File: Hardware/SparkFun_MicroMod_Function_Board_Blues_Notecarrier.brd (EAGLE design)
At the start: 37.5 x 65 mm, 85 parts, among them J2 MICROMOD_FUNCTION_STANDARD, J6 NOTECARD, Q1 5.8A/30V/35mΩ, Q2 20V/4.2A/52mΩ/1.4W, Q3 5.8A/30V/35mΩ, Q4 20V/4.2A/52mΩ/1.4W, U1 EEPROM, U2 TCR2EF33

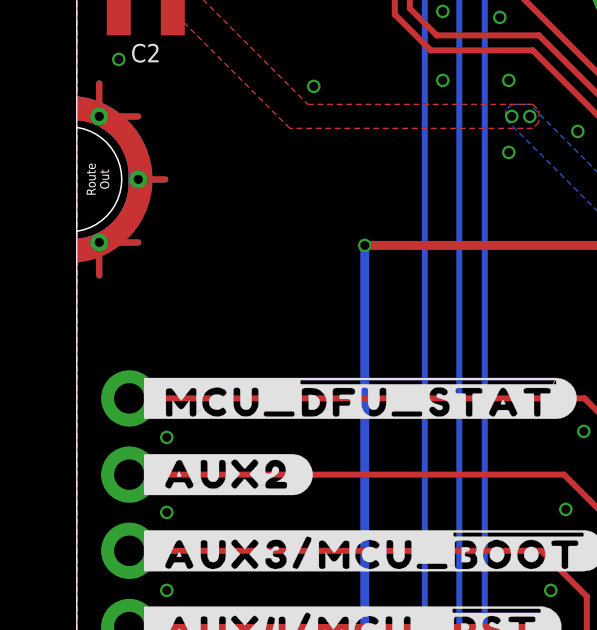
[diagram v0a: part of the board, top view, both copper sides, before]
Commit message: Added micromod silks.
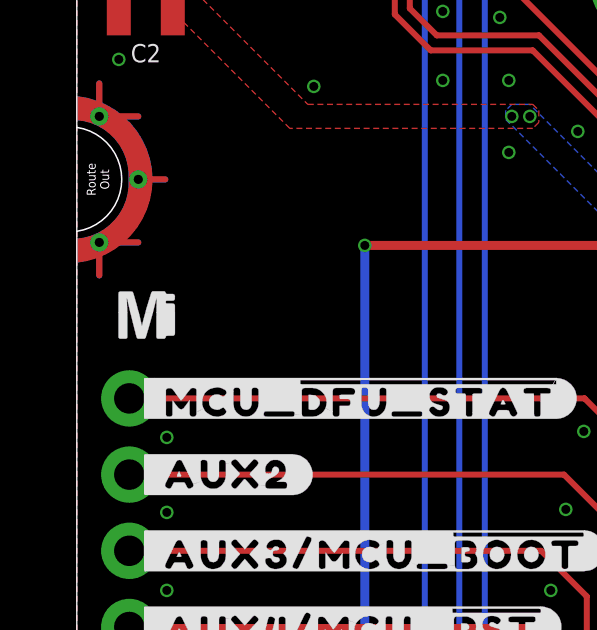
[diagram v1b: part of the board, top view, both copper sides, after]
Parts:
- added U$29: (no value), SparkFun-MicroMod:MICROMOD_MI_LOGO_.35
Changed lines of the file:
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@@
 <element name="U$27" library="output" package="#AUX1#MCU_#DFU_STAT##0" value="" x="21.2" y="36.7" smashed="yes" rot="MR0"/>
 <element name="U$28" library="SparkFun-MicroMod" package="MICROMOD_LOGO_.3" value="" x="20.2" y="41.1" smashed="yes" rot="MR0"/>
+<element name="U$29" library="SparkFun-MicroMod" package="MICROMOD_MI_LOGO_.35" value="" x="2.3" y="39.5" smashed="yes"/>
 </elements>
 <signals>

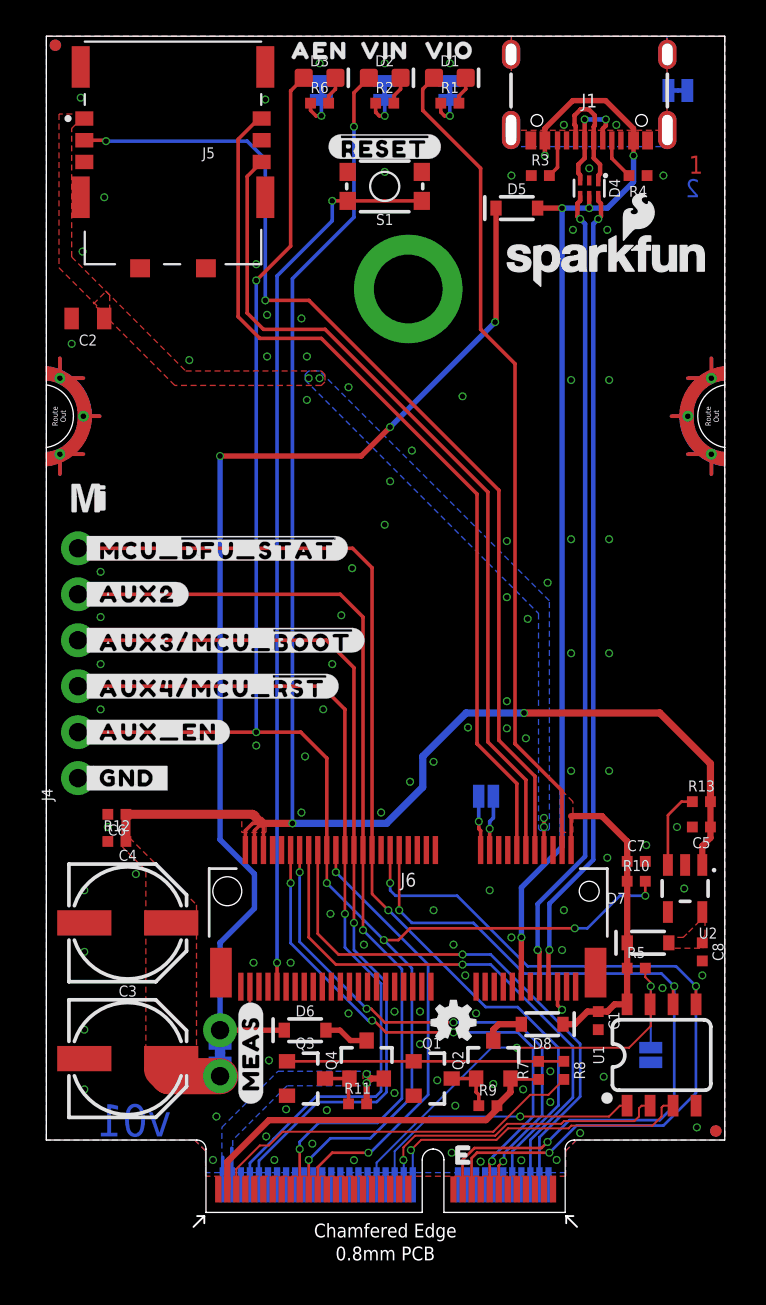
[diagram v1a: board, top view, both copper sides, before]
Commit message: Post DR updates.
Schematic:
Add Text to VREG
Add Text to Notecard
add 100 ohm resistor on pwr ctrl
Change Q1/Q3 transistors
Add Text to jumpers
Move V_USB on Notecard

Board:
Remove L2/L15
Add units for measures
Remove underscores from Silks
Move EWP via over
Remove copper layer notes
Give silk labels correct pointers
Increase mask stop on pads to ensure isolation
Move V_USB via down to allow ground pour
Check Wire stubs
Move 3.3V up to pour gnd better
Redo measures to make them look nice
Move some vias around to pour ground better
Place 100 ohm resistors
Place InRush current limiting resistor
Reroute
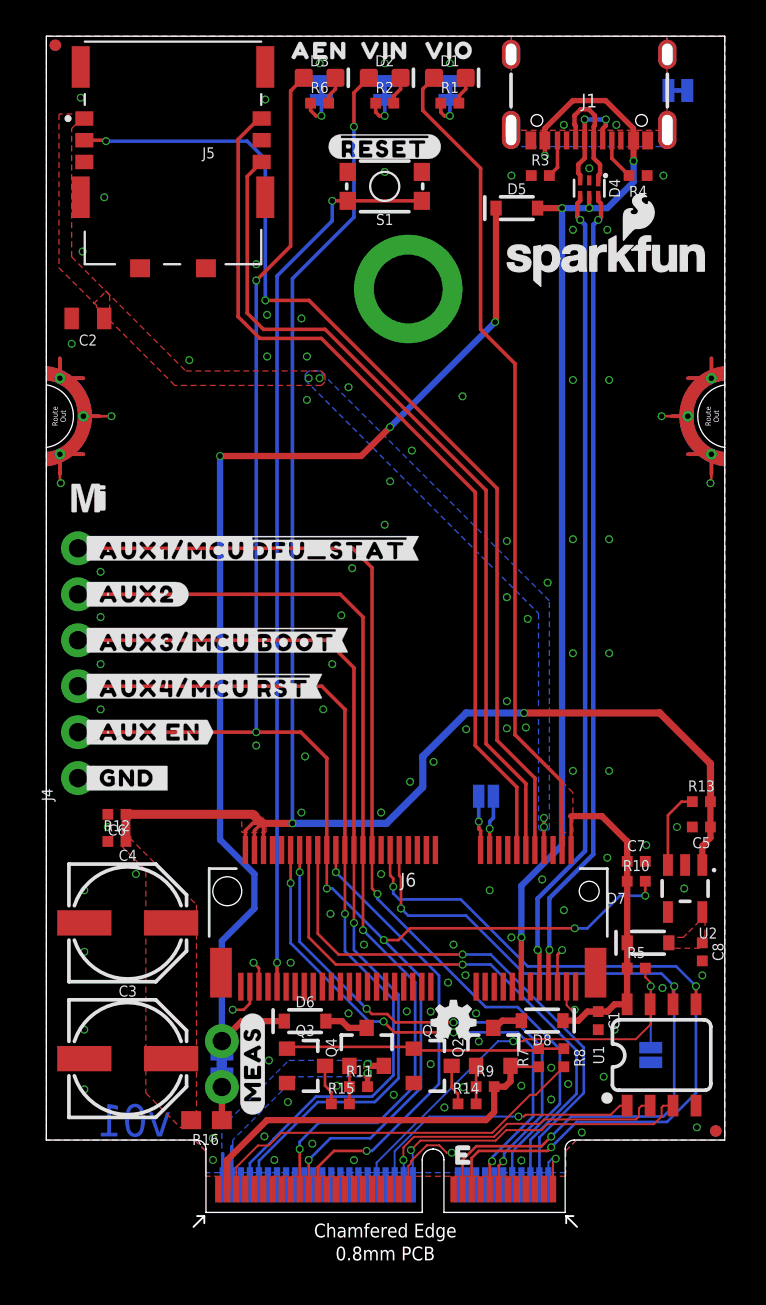
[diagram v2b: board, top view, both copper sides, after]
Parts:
- removed U$23: (no value), output:#AUX_EN_#25
- added R14, R15: 100, SparkFun-Resistors:0402-TIGHT
- added R16: 1, SparkFun-Resistors:0603
- added U$30: (no value), output:#AUX_EN_#0
- Q1, Q3: value 5.8A/30V/35mΩ -> 220mA/50V/3.5Ω
- U$12: device output:#_MCU_#DFU_STAT##0 -> output:#_AUX1#MCU_#DFU_STAT##0
- moved R9 1.06 mm to (24.2, 6.95)
- moved R11 0.95 mm to (17.2, 6.95)
- moved U$25 0.90 mm to (16.4, 31.6)
- moved U$24 0.90 mm to (15.0, 29.1)
- moved U$27 0.90 mm to (20.3, 36.7)
- moved R7 0.70 mm to (27.2, 8.55)
- moved R8 0.70 mm to (28.6, 8.55)
- moved Q1 0.70 mm to (21.3, 8.10)
- moved Q2 0.70 mm to (24.7, 9.10)
- moved Q3 0.70 mm to (14.3, 8.10)
- moved Q4 0.70 mm to (17.7, 9.10)
- moved MEAS 0.61 mm to (9.70, 8.20)
- moved U$17 0.61 mm to (11.4, 8.20)
- moved D6 0.50 mm to (14.3, 10.6)
- moved D8 0.20 mm to (27.4, 10.6)
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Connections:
- new net N$15: Q1.3, R14.1
- new net N$16: Q3.3, R15.1
- new net N$17: MEAS.2, MEAS.4, R16.1
- net N$2: now also R14.2; no longer Q1.3
- net N$3: now also R15.2; no longer Q3.3
- net VIN: now also R16.2; no longer MEAS.2, MEAS.4
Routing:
- net GND: track 2.86 -> 21.3 mm, vias 109 -> 116
- net VIN: track 96.8 -> 92.7 mm
- net N$17: track 0.00 -> 2.59 mm
- net N$15: track 0.00 -> 2.24 mm
- net N$16: track 0.00 -> 2.24 mm
- net 3V3_IN: track 21.2 -> 22.3 mm
- net N$37: track 62.2 -> 63.1 mm
- net N$2: track 2.91 -> 2.10 mm
- net N$3: track 2.77 -> 2.10 mm
- net AUX2: track 53.0 -> 53.6 mm
- net AUX_EN: track 97.3 -> 97.9 mm
- net N$7: track 2.27 -> 1.72 mm
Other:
- board text added: "All units in mm."
- board text removed: "1"
- board text removed: "2"
